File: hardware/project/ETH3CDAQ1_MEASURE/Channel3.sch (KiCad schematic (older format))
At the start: 49 parts, among them U1501 LT1355, U1502 DG211, U1503 DG419LDY, U1504 DG419LDY, U1505 OPA192, U1506 74LVC1GU04DRL, U1507 ADS8681RUM, U1508 74HCT595

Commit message: PCB design
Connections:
- net +5VF is gone; now on net +5V: U1507.16 (AVDD)
- net CH2_IN renamed CH3_IN
- net DAC_V2 renamed DAC_V3
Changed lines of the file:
@@
 	11200 5050 11200 5000
 Text HLabel 2800 6150 0    50   Input ~ 0
-DAC_V2
+DAC_V3
 Wire Wire Line
 	2800 6150 2850 6150
@@
 Connection ~ 9950 5900
 Text HLabel 2800 4750 0    50   Input ~ 0
-CH2_IN
+CH3_IN
 $Comp
 L ETH3CDAQ1:+18V #PWR?
@@
 Wire Wire Line
 	4450 10600 4700 10600
-$Comp
-L ETH3CDAQ1:+5VF #PWR?
-U 1 1 5FC0EABD
-P 12100 4100
-AR Path="/5FB85416/5FC0EABD" Ref="#PWR?"  Part="1"
-AR Path="/5FF801EB/5FC0EABD" Ref="#PWR?"  Part="1"
-AR Path="/5FBD66F6/5FC0EABD" Ref="#PWR01538"  Part="1"
-F 0 "#PWR01538" H 12100 3950 50  0001 C CNN
-F 1 "+5VF" H 12115 4273 50  0000 C CNN
-F 2 "" H 12100 4100 50  0001 C CNN
-F 3 "" H 12100 4100 50  0001 C CNN
-	1    12100 4100
-	1    0    0    -1
-$EndComp
 Wire Wire Line
 	11750 4650 11200 4650
@@
 SR2_QH
 NoConn ~ 12450 6950
+$Comp
+L power:+5V #PWR0102
+U 1 1 5FD9494B
+P 12100 4100
+F 0 "#PWR0102" H 12100 3950 50  0001 C CNN
+F 1 "+5V" H 12115 4273 50  0000 C CNN
+F 2 "" H 12100 4100 50  0001 C CNN
+F 3 "" H 12100 4100 50  0001 C CNN
+	1    12100 4100
+	1    0    0    -1
+$EndComp
 $EndSCHEMATC

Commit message: PCB layout
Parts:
- added R806: 0, Resistor_SMD:R_0603_1608Metric_Pad0.98x0.95mm_HandSolder, symbol Device:R
- renumbered C1501 to C801, C1502 to C802, C1503 to C803, C1504 to C804, C1505 to C805, C1506 to C806, C1507 to C807, C1508 to C808, C1509 to C809, C1510 to C810, C1511 to C811, C1512 to C812, C1513 to C813, C1514 to C814, C1515 to C815, C1516 to C816, C1517 to C817, C1518 to C818, C1519 to C819, C1520 to C820, C1521 to C821, C1522 to C822, C1523 to C823, C1524 to C824, C1525 to C825, R1501 to R801, R1502 to R802, R1503 to R803, R1504 to R804, R1505 to R805, R1506 to R807, R1507 to R808, R1508 to R809, R1509 to R810, R1510 to R811, R1511 to R812, R1512 to R813, R1513 to R814, R1514 to R815, R1515 to R816, R1516 to R817, U1501 to U801, U1502 to U802, U1503 to U803, U1504 to U804, U1505 to U805, U1506 to U806, U1507 to U807, U1508 to U808
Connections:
- net at U802.10, U802.15, U802.3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: now also R806.2
- net at U803.1, U805.3 (+), U805.6: now also R806.1

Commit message: Fixed mistake with DG419. Never use DG419Lxx variant.
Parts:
- U803, U804: value DG419LDY -> DG419DY; symbol Analog_Switch:DG419LDY -> Analog_Switch:DG419xY
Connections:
- net at R806.2, U802.10, U802.15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: now also U805.3 (+); no longer U805.2 (-)
- net at R806.1, U803.1, U805.6: now also U805.2 (-); no longer U805.3 (+)
- no-connect marks 8 -> 10
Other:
- note added: "RN - CAY10-681J4LF"
- note removed: "RN - ACASA1001S1001P100"
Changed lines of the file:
@@
 $EndDescr
 Text Notes 3800 8300 0    50   ~ 0
-RN -  ACASA1001S1001P100
+RN -  CAY10-681J4LF
 $Comp
 L ETH3CDAQ1:DG211 U?
@@
 $EndComp
 $Comp
-L Analog_Switch:DG419LDY U?
+L Analog_Switch:DG419xY U?
 U 2 1 5FC0E887
 P 2350 10100
@@
 AR Path="/5FBD66F6/5FC0E887" Ref="U803"  Part="2"
 F 0 "U803" H 2630 10146 50  0000 L CNN
-F 1 "DG419LDY" H 2630 10055 50  0000 L CNN
+F 1 "DG419DY" H 2630 10055 50  0000 L CNN
 F 2 "Package_SO:SOIC-8_3.9x4.9mm_P1.27mm" H 2350 9800 50  0001 C CNN
 F 3 "https://datasheets.maximintegrated.com/en/ds/DG417-DG419.pdf" H 2350 10100 50  0001 C CNN
@@
 $EndComp
 $Comp
-L Analog_Switch:DG419LDY U?
+L Analog_Switch:DG419xY U?
 U 2 1 5FC0E88D
 P 3200 10100
@@
 AR Path="/5FBD66F6/5FC0E88D" Ref="U804"  Part="2"
 F 0 "U804" H 3480 10146 50  0000 L CNN
-F 1 "DG419LDY" H 3480 10055 50  0000 L CNN
+F 1 "DG419DY" H 3480 10055 50  0000 L CNN
 F 2 "Package_SO:SOIC-8_3.9x4.9mm_P1.27mm" H 3200 9800 50  0001 C CNN
 F 3 "https://datasheets.maximintegrated.com/en/ds/DG417-DG419.pdf" H 3200 10100 50  0001 C CNN
@@
 $EndComp
 $Comp
-L Analog_Switch:DG419LDY U?
+L Analog_Switch:DG419xY U?
 U 1 1 5FC0E905
 P 5600 4550
@@
 AR Path="/5FBD66F6/5FC0E905" Ref="U803"  Part="1"
 F 0 "U803" H 5600 4792 50  0000 C CNN
-F 1 "DG419LDY" H 5600 4701 50  0000 C CNN
+F 1 "DG419DY" H 5600 4701 50  0000 C CNN
 F 2 "Package_SO:SOIC-8_3.9x4.9mm_P1.27mm" H 5600 4250 50  0001 C CNN
 F 3 "https://datasheets.maximintegrated.com/en/ds/DG417-DG419.pdf" H 5600 4550 50  0001 C CNN
@@
 $EndComp
 $Comp
-L Analog_Switch:DG419LDY U?
+L Analog_Switch:DG419xY U?
 U 1 1 5FC0E90B
 P 9950 4550
@@
 AR Path="/5FBD66F6/5FC0E90B" Ref="U804"  Part="1"
 F 0 "U804" H 9950 4792 50  0000 C CNN
-F 1 "DG419LDY" H 9950 4701 50  0000 C CNN
+F 1 "DG419DY" H 9950 4701 50  0000 C CNN
 F 2 "Package_SO:SOIC-8_3.9x4.9mm_P1.27mm" H 9950 4250 50  0001 C CNN
 F 3 "https://datasheets.maximintegrated.com/en/ds/DG417-DG419.pdf" H 9950 4550 50  0001 C CNN
@@
 Wire Wire Line
 	13700 4150 13900 4150
-$Comp
-L ETH3CDAQ1:OPA192 U?
-U 1 1 5FC0EB2A
-P 4750 4650
-AR Path="/5FB85416/5FC0EB2A" Ref="U?"  Part="1"
-AR Path="/5FF801EB/5FC0EB2A" Ref="U?"  Part="1"
-AR Path="/5FBD66F6/5FC0EB2A" Ref="U805"  Part="1"
-F 0 "U805" H 4850 4900 50  0000 L CNN
-F 1 "OPA192" H 4800 4800 50  0000 L CNN
-F 2 "Package_SO:SOIC-8_3.9x4.9mm_P1.27mm" H 4800 4700 50  0001 C CNN
-F 3 "" H 4800 4800 50  0001 C CNN
-	1    4750 4650
-	1    0    0    -1
-$EndComp
 Wire Wire Line
 	4450 4550 4400 4550
@@
 L ETH3CDAQ1:+18V #PWR?
 U 1 1 5FC0EB35
-P 4650 4350
+P 4650 4950
 AR Path="/5FB85416/5FC0EB35" Ref="#PWR?"  Part="1"
 AR Path="/5FF801EB/5FC0EB35" Ref="#PWR?"  Part="1"
 AR Path="/5FBD66F6/5FC0EB35" Ref="#PWR0818"  Part="1"
-F 0 "#PWR0818" H 4650 4200 50  0001 C CNN
-F 1 "+18V" H 4665 4523 50  0000 C CNN
-F 2 "" H 4650 4350 50  0001 C CNN
-F 3 "" H 4650 4350 50  0001 C CNN
-	1    4650 4350
-	1    0    0    -1
-$EndComp
-$Comp
-L ETH3CDAQ1:-18V #PWR?
-U 1 1 5FC0EB3B
-P 4650 4950
-AR Path="/5FB85416/5FC0EB3B" Ref="#PWR?"  Part="1"
-AR Path="/5FF801EB/5FC0EB3B" Ref="#PWR?"  Part="1"
-AR Path="/5FBD66F6/5FC0EB3B" Ref="#PWR0819"  Part="1"
-F 0 "#PWR0819" H 4650 4800 50  0001 C CNN
-F 1 "-18V" H 4665 5123 50  0000 C CNN
+F 0 "#PWR0818" H 4650 4800 50  0001 C CNN
+F 1 "+18V" H 4665 5123 50  0000 C CNN
 F 2 "" H 4650 4950 50  0001 C CNN
 F 3 "" H 4650 4950 50  0001 C CNN
 	1    4650 4950
 	-1   0    0    1
+$EndComp
+$Comp
+L ETH3CDAQ1:-18V #PWR?
+U 1 1 5FC0EB3B
+P 4650 4350
+AR Path="/5FB85416/5FC0EB3B" Ref="#PWR?"  Part="1"
+AR Path="/5FF801EB/5FC0EB3B" Ref="#PWR?"  Part="1"
+AR Path="/5FBD66F6/5FC0EB3B" Ref="#PWR0819"  Part="1"
+F 0 "#PWR0819" H 4650 4200 50  0001 C CNN
+F 1 "-18V" H 4665 4523 50  0000 C CNN
+F 2 "" H 4650 4350 50  0001 C CNN
+F 3 "" H 4650 4350 50  0001 C CNN
+	1    4650 4350
+	1    0    0    -1
 $EndComp
 Wire Wire Line
@@
 Wire Wire Line
 	5150 5450 5150 4650
+NoConn ~ 4750 4350
+NoConn ~ 4750 4950
+$Comp
+L ETH3CDAQ1:OPA192 U?
+U 1 1 5FC0EB2A
+P 4750 4650
+AR Path="/5FB85416/5FC0EB2A" Ref="U?"  Part="1"
+AR Path="/5FF801EB/5FC0EB2A" Ref="U?"  Part="1"
+AR Path="/5FBD66F6/5FC0EB2A" Ref="U805"  Part="1"
+F 0 "U805" H 4850 4400 50  0000 L CNN
+F 1 "OPA192" H 4800 4500 50  0000 L CNN
+F 2 "Package_SO:SOIC-8_3.9x4.9mm_P1.27mm" H 4800 4700 50  0001 C CNN
+F 3 "" H 4800 4800 50  0001 C CNN
+	1    4750 4650
+	1    0    0    1
+$EndComp
 $EndSCHEMATC

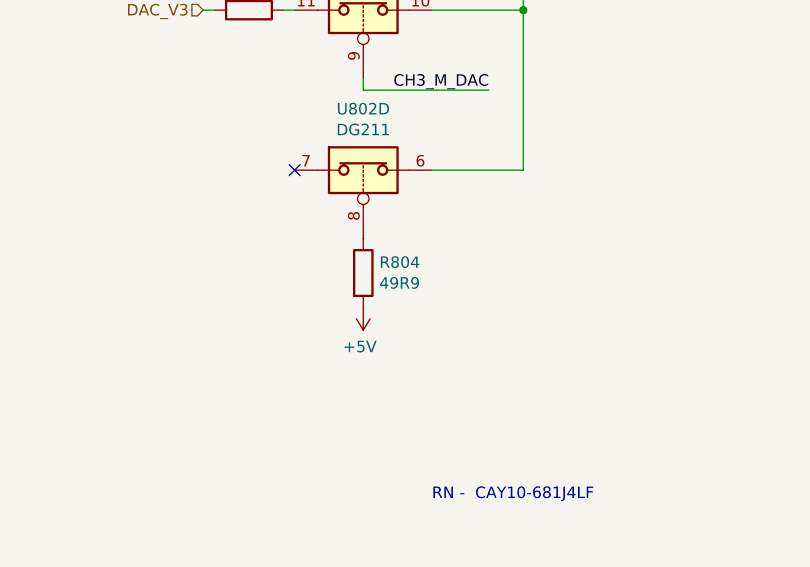
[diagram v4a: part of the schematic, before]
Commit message: STM32H7+FreeRTOS+LwIP works, thanks to this guide https://community.st.com/s/article/How-to-create-project-for-STM32H7-with-Ethernet-and-LwIP-stack-working. Add a 100ms delay before LWiP Init function.
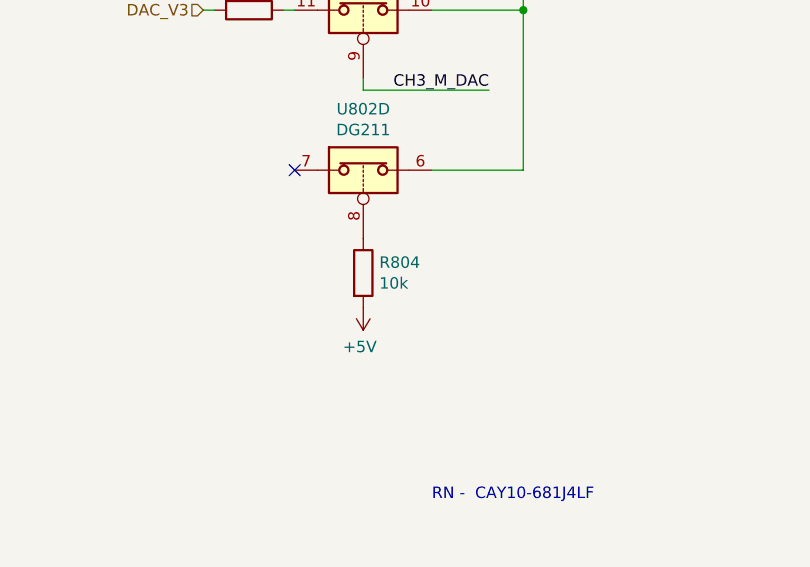
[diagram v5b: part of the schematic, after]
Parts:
- R804: value 49R9 -> 10k
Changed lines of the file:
@@
 AR Path="/5FBD66F6/5FC0EA41" Ref="R804"  Part="1"
 F 0 "R804" H 3570 7346 50  0000 L CNN
-F 1 "49R9" H 3570 7255 50  0000 L CNN
+F 1 "10k" H 3570 7255 50  0000 L CNN
 F 2 "Resistor_SMD:R_0603_1608Metric_Pad0.98x0.95mm_HandSolder" V 3430 7300 50  0001 C CNN
 F 3 "~" H 3500 7300 50  0001 C CNN
